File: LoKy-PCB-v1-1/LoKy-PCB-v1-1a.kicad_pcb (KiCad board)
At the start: 2 copper layers, 23 parts, among them P1 HEADER_M_2.54MM_1R3P_ST_AU_PTH, P2 HEADER_M_2.54MM_1R3P_ST_AU_PTH, U1 RFM95, U2 ARDUINO_PRO_MINI

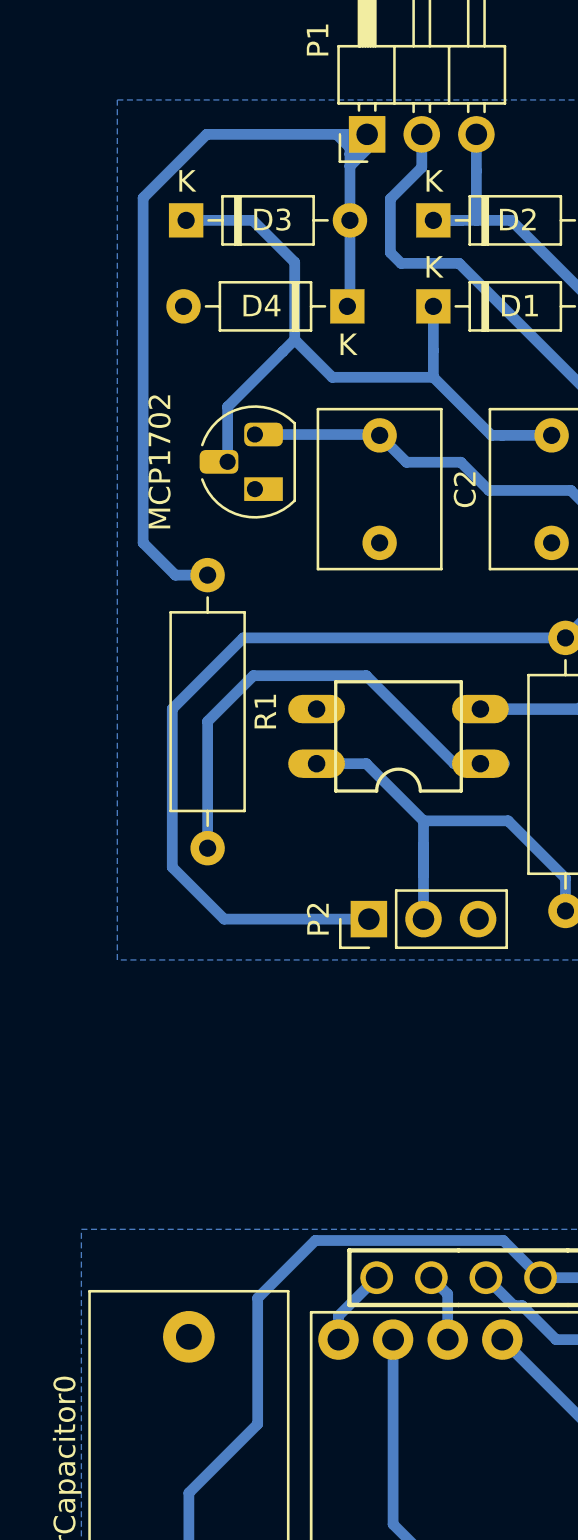
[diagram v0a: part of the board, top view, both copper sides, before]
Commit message: Update KiCAD library
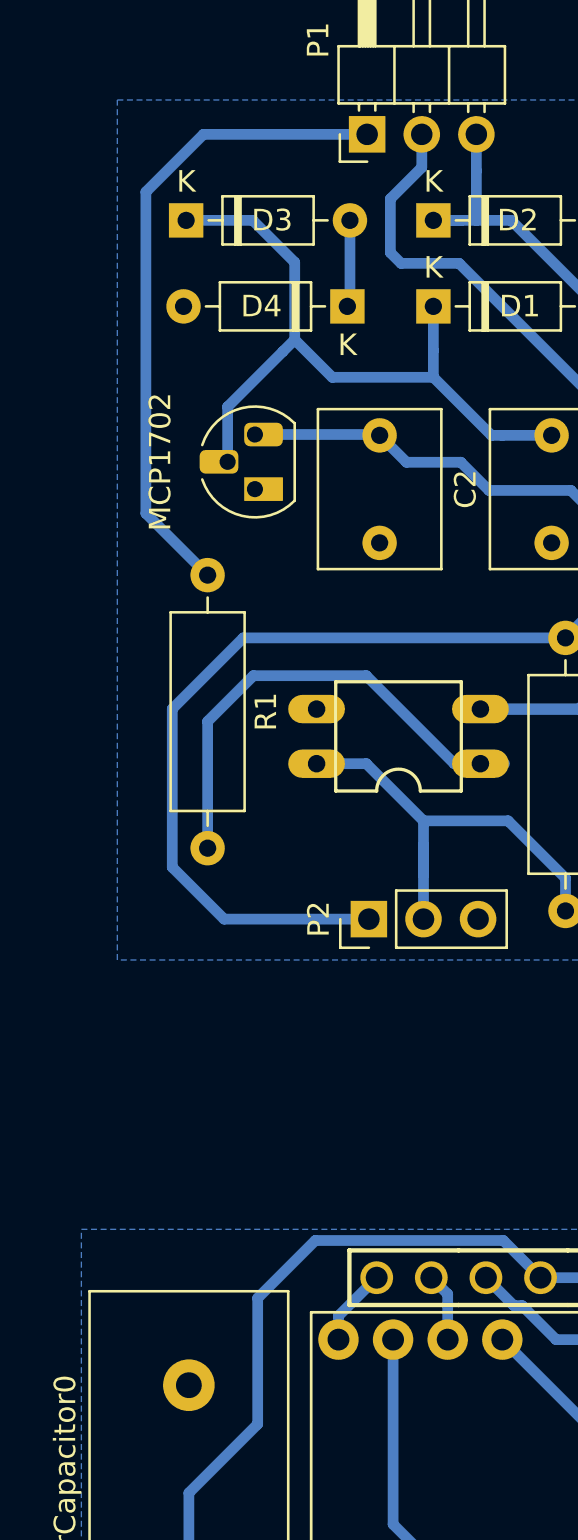
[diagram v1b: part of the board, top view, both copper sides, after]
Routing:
- net I1: track 42.8 -> 34.5 mm
